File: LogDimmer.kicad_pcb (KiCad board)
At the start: 2 copper layers, 33 x 19 mm, 19 parts, among them J1 Conn_01x02, J2 LED-PSU, J3 POT, U1 L78L33_SOT89, U2 PC817X3, U3 ATtiny13A-SS

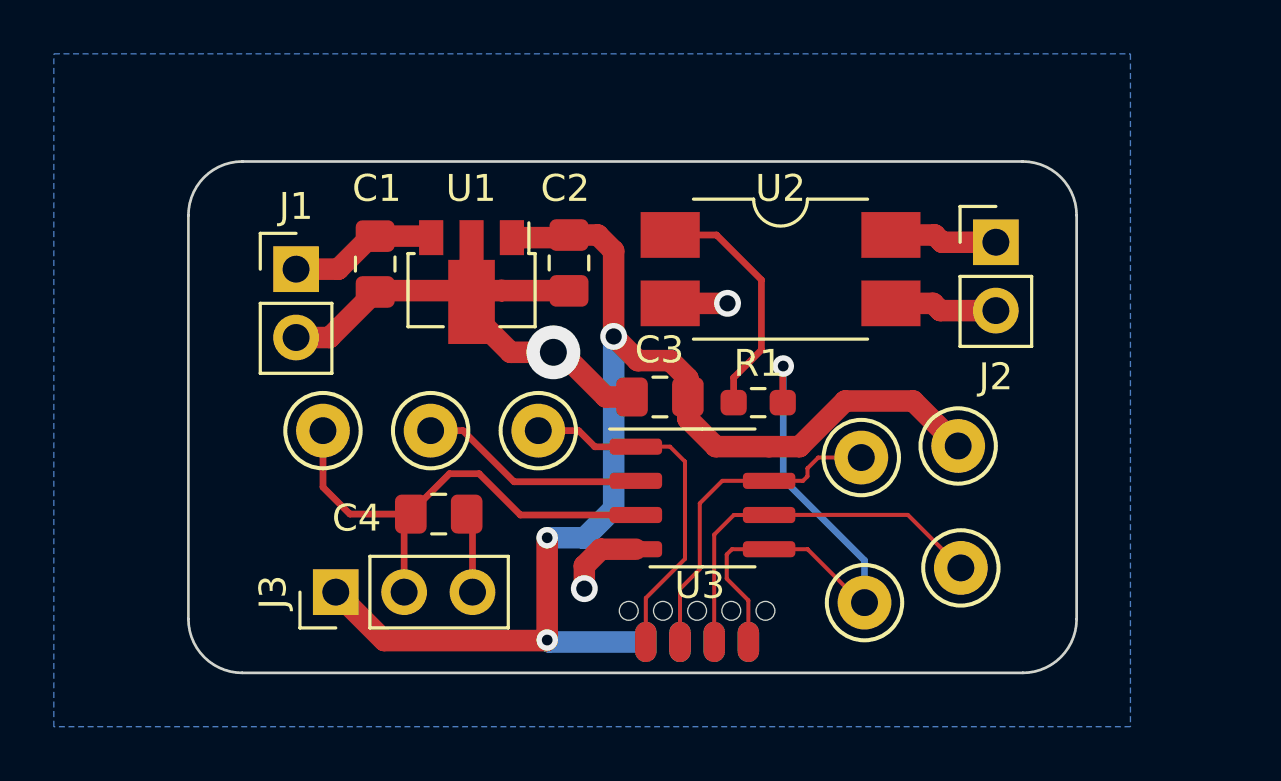
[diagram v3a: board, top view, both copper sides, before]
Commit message: Removing attempts at including hash, adding mount holes to schematic
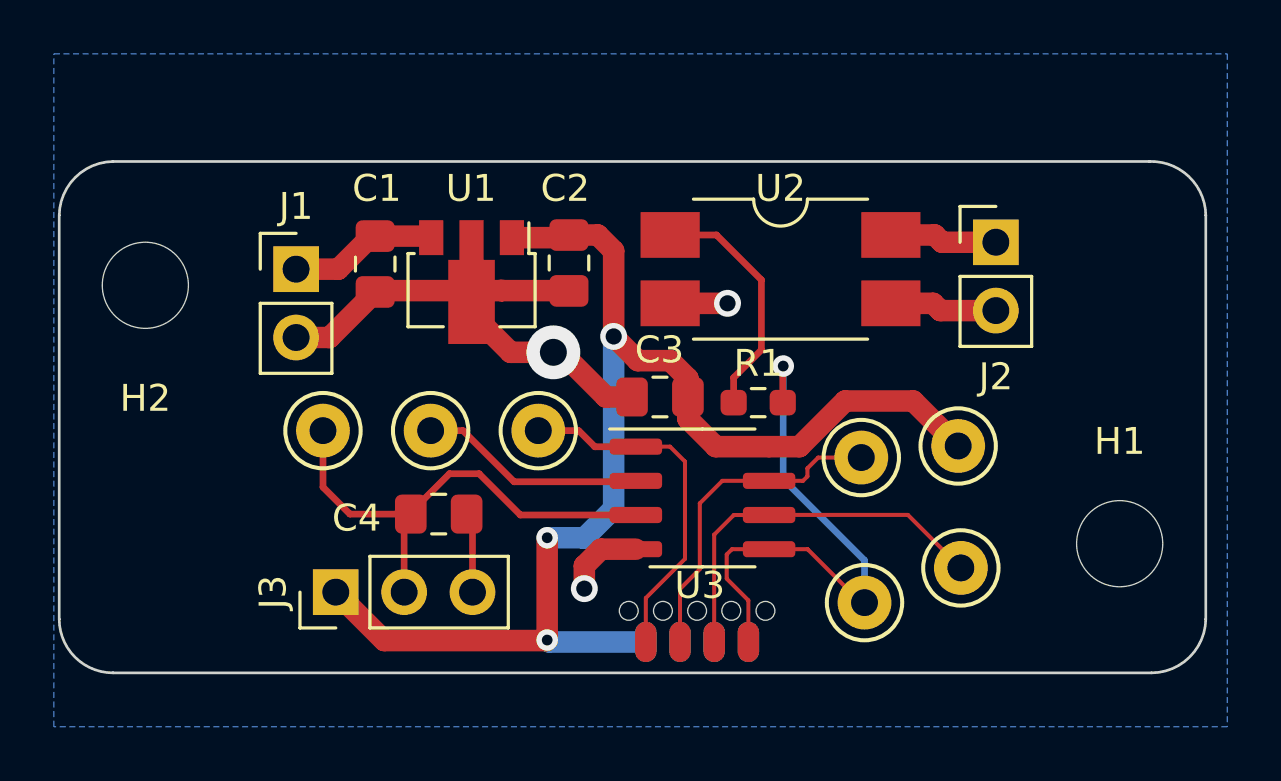
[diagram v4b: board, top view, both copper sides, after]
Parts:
- added H1: MountingHole, MountingHole:MountingHole_3.2mm_M3_DIN965, F.Cu at (184.6, 93.2)
- added H2: MountingHole, MountingHole:MountingHole_3.2mm_M3_DIN965, F.Cu at (148.4, 83.6)
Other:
- board size 33 x 19 mm -> 42.6 x 19 mm
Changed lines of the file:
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@@
     )
+  )
+  (footprint "MountingHole:MountingHole_3.2mm_M3_DIN965" (layer "F.Cu")
+    (at 148.4 83.6)
+    (descr "Mounting Hole 3.2mm, no annular, M3, DIN965")
+    (tags "mounting hole 3.2mm no annular m3 din965")
+    (property "Sheetfile" "LogDimmer.kicad_sch")
+    (property "Sheetname" "")
+    (attr exclude_from_pos_files)
+    (fp_text reference "H2" (at 0 4.2) (layer "F.SilkS")
+      (effects (font (size 1 1) (thickness 0.15)))
+    )
+    (fp_text value "MountingHole" (at 0 3.8) (layer "F.Fab")
+      (effects (font (size 1 1) (thickness 0.15)))
+    )
+    (fp_text user "${REFERENCE}" (at 0 0) (layer "F.Fab")
+      (effects (font (size 1 1) (thickness 0.15)))
+    )
+    (fp_circle (center 0 0) (end 2.8 0) (layer "Cmts.User") (width 0.15) (fill none))
+    (fp_circle (center 0 0) (end 3.05 0) (layer "F.CrtYd") (width 0.05) (fill none))
+    (pad "" np_thru_hole circle (at 0 0) (size 3.2 3.2) (drill 3.2) (layers *.Cu *.Mask))
   )
   (footprint "Package_SO:SOIC-8_3.9x4.9mm_P1.27mm" (layer "F.Cu")
@@
       (rotate (xyz 0 0 0))
     )
+  )
+  (footprint "MountingHole:MountingHole_3.2mm_M3_DIN965" (layer "F.Cu")
+    (at 184.6 93.2)
+    (descr "Mounting Hole 3.2mm, no annular, M3, DIN965")
+    (tags "mounting hole 3.2mm no annular m3 din965")
+    (property "Sheetfile" "LogDimmer.kicad_sch")
+    (property "Sheetname" "")
+    (attr exclude_from_pos_files)
+    (fp_text reference "H1" (at 0 -3.8) (layer "F.SilkS")
+      (effects (font (size 1 1) (thickness 0.15)))
+    )
+    (fp_text value "MountingHole" (at 0 3.8) (layer "F.Fab")
+      (effects (font (size 1 1) (thickness 0.15)))
+    )
+    (fp_text user "${REFERENCE}" (at 0 0) (layer "F.Fab")
+      (effects (font (size 1 1) (thickness 0.15)))
+    )
+    (fp_circle (center 0 0) (end 2.8 0) (layer "Cmts.User") (width 0.15) (fill none))
+    (fp_circle (center 0 0) (end 3.05 0) (layer "F.CrtYd") (width 0.05) (fill none))
+    (pad "" np_thru_hole circle (at 0 0) (size 3.2 3.2) (drill 3.2) (layers *.Cu *.Mask))
   )
   (footprint "TestPoint:TestPoint_Keystone_5000-5004_Miniature" (layer "F.Cu")
@@
   (gr_line (start 155.5 80.375) (end 165.5 80.375) (layer "B.SilkS") (width 0.4))
   (gr_line (start 165.5 80.375) (end 165.5 84.625) (layer "B.SilkS") (width 0.4))
-  (gr_arc (start 152 98) (mid 150.585786 97.414214) (end 150 96) (layer "Edge.Cuts") (width 0.1))
-  (gr_line (start 183 81) (end 183 96) (layer "Edge.Cuts") (width 0.1))
-  (gr_arc (start 150 81) (mid 150.585786 79.585786) (end 152 79) (layer "Edge.Cuts") (width 0.1))
-  (gr_arc (start 181 79) (mid 182.414214 79.585786) (end 183 81) (layer "Edge.Cuts") (width 0.1))
-  (gr_line (start 181 98) (end 152 98) (layer "Edge.Cuts") (width 0.1))
-  (gr_line (start 152 79) (end 181 79) (layer "Edge.Cuts") (width 0.1))
-  (gr_line (start 150 96) (end 150 81) (layer "Edge.Cuts") (width 0.1))
-  (gr_arc (start 183 96) (mid 182.414214 97.414214) (end 181 98) (layer "Edge.Cuts") (width 0.1))
+  (gr_arc (start 147.2 98) (mid 145.785786 97.414214) (end 145.2 96) (layer "Edge.Cuts") (width 0.1))
+  (gr_line (start 187.8 81) (end 187.8 96) (layer "Edge.Cuts") (width 0.1))
+  (gr_arc (start 145.2 81) (mid 145.794088 79.594088) (end 147.2 79) (layer "Edge.Cuts") (width 0.1))
+  (gr_arc (start 185.7 79) (mid 187.170185 79.558806) (end 187.8 81) (layer "Edge.Cuts") (width 0.1))
+  (gr_line (start 185.785786 98) (end 147.2 98) (layer "Edge.Cuts") (width 0.1))
+  (gr_line (start 147.2 79) (end 185.7 79) (layer "Edge.Cuts") (width 0.1))
+  (gr_line (start 145.2 96) (end 145.2 81) (layer "Edge.Cuts") (width 0.1))
+  (gr_arc (start 187.8 96) (mid 187.200868 97.410875) (end 185.785786 98) (layer "Edge.Cuts") (width 0.1))
   (gr_text "LogDimmer\nBESearle 2022" (at 178.25 82.75) (layer "B.SilkS")
     (effects (font (size 1.5 1) (thickness 0.25)) (justify left mirror))
@@
   )
   (dimension (type aligned) (layer "F.Fab")
-    (pts (xy 181 79) (xy 181 98))
+    (pts (xy 185.7 79) (xy 185.785786 98))
     (height -10.3)
-    (gr_text "19.0000 mm" (at 190.15 88.5 90) (layer "F.Fab")
+    (gr_text "19.0002 mm" (at 197.192776 88.448303 270.2586917) (layer "F.Fab")
       (effects (font (size 1 1) (thickness 0.15)))
     )
@@
   )
   (dimension (type aligned) (layer "F.Fab")
-    (pts (xy 150 81) (xy 183 81))
+    (pts (xy 145.2 81) (xy 187.8 81))
     (height -5.8)
-    (gr_text "33.0000 mm" (at 166.5 74.05) (layer "F.Fab")
+    (gr_text "42.6000 mm" (at 166.5 74.05) (layer "F.Fab")
       (effects (font (size 1 1) (thickness 0.15)))
     )
@@
     (polygon
       (pts
-        (xy 186.5 87.5)
+        (xy 189.7 87.5)
         (xy 177 87.5)
         (xy 177 78.5)
-        (xy 186.5 78.5)
+        (xy 189.7 78.5)
       )
     )
@@
     (polygon
       (pts
-        (xy 185 100)
+        (xy 188.6 100)
         (xy 145 100)
         (xy 145 75)
-        (xy 185 75)
+        (xy 188.6 75)
       )
     )
